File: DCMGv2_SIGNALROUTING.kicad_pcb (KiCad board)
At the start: 2 copper layers, 271.3 x 163.1 mm, 308 parts, among them P1 BRANCH 1 BUS 1 LOAD3 NC, P10 BRANCH 1 BUS 1 LOAD 2 NC, P100 CONNECTOR, P101 CONNECTOR, P102 CONNECTOR, P103 CONNECTOR, P104 CONNECTOR, P105 CONNECTOR, P106 CONNECTOR, P107 CONNECTOR, P108 CONNECTOR, P109 CONNECTOR, P11 BRANCH 1 BUS 1 LOAD 1 NO, P110 CONNECTOR, P111 CONNECTOR, P112 CONNECTOR, P113 CONNECTOR, P114 CONNECTOR, P115 CONNECTOR, P116 CONNECTOR, P117 CONNECTOR, P118 CONNECTOR, P119 CONNECTOR, P12 BRANCH 1 BUS 1 LOAD 1 NC, P120 CONNECTOR, P121 CONNECTOR, P122 CONNECTOR, P123 CONNECTOR, P124 CONNECTOR, P125 CONNECTOR, P126 CONNECTOR, P127 CONNECTOR, P128 CONNECTOR, P129 CONNECTOR, P13 BRANCH 2 BUS 1 LOAD 1 NO, P130 CONNECTOR, P131 CONNECTOR, P132 CONNECTOR, P133 CONNECTOR, P134 CONNECTOR, P135 CONNECTOR, P136 CONNECTOR, P137 CONNECTOR, P138 CONNECTOR, P139 CONNECTOR, P14 BRANCH 2 BUS 1 DISTAL NC, P140 CONNECTOR, P141 CONNECTOR, P142 CONNECTOR, P143 CONNECTOR, P144 CONNECTOR, P145 CONNECTOR, P146 CONNECTOR, P147 CONNECTOR, P148 CONNECTOR, P149 CONNECTOR, P15 BRANCH 2 BUS 1 DISTAL USER, P150 CONNECTOR, P151 CONNECTOR, P152 CONNECTOR, P153 CONNECTOR, P154 CONNECTOR, P155 CONNECTOR, P156 CONNECTOR, P157 CONNECTOR, P158 CONNECTOR, P159 CONNECTOR, P16 BRANCH 2 BUS 1 DISTAL NO, P160 CONNECTOR, P161 CONNECTOR, P162 CONNECTOR, P163 CONNECTOR, P164 CONNECTOR, P165 CONNECTOR, P166 CONNECTOR, P167 CONNECTOR, P168 CONNECTOR, P169 CONNECTOR, P17 BRANCH 2 BUS 1 PROXIMAL NC, P170 CONNECTOR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

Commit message: most traces are triple thickness
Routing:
- net N-0000087: track 55.7 -> 50.0 mm
- net N-0000069: track 50.5 -> 45.2 mm
- net N-0000043: track 139.6 -> 144.6 mm
- net N-0000068: track 67.3 -> 64.8 mm
- net N-0000058: track 92.1 -> 90.0 mm
- net N-0000057: track 91.6 -> 89.9 mm
- net N-0000036: track 89.6 -> 88.3 mm
- net N-0000039: track 90.9 -> 89.7 mm
- net N-0000035: track 89.7 -> 88.5 mm
- net N-0000037: track 89.3 -> 88.3 mm
- net N-0000033: track 91.2 -> 90.1 mm
- net N-0000032: track 91.6 -> 90.6 mm
- net N-0000047: track 91.8 -> 91.0 mm
- net N-0000089: track 34.0 -> 33.4 mm
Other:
- net class thick_signal added: clearance 0.254, trace_width 0.766, via_dia 0.889, via_drill 0.635

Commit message: all traces triple thickness. improved routing
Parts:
- moved P108 7.62 mm to (149.6, 167.4)
- moved P109 7.62 mm to (152.1, 167.4)
- moved P110 7.62 mm to (154.7, 167.4)
- moved P111 7.62 mm to (157.2, 167.4)
- moved P112 7.62 mm to (159.8, 167.4)
- moved P113 7.62 mm to (162.3, 167.4)
- moved P114 7.62 mm to (164.8, 167.4)
- moved P115 7.62 mm to (167.4, 167.4)
- moved P116 7.62 mm to (169.9, 167.4)
- moved P117 7.62 mm to (172.5, 167.4)
- moved P118 7.62 mm to (175.0, 167.4)
- moved P119 7.62 mm to (177.5, 167.4)
- moved P120 7.62 mm to (180.1, 167.4)
- moved P121 7.62 mm to (182.6, 167.4)
- moved P122 7.62 mm to (185.2, 167.4)
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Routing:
- net N-0000059: track 126.2 -> 137.2 mm
- net N-0000042: track 79.3 -> 70.1 mm
- net N-00000131: track 81.1 -> 72.1 mm
- net N-0000044: track 94.5 -> 85.6 mm
- net N-00000122: track 81.4 -> 73.0 mm
- net N-0000040: track 93.3 -> 85.6 mm
- net N-0000045: track 92.8 -> 85.6 mm
- net N-0000047: track 91.0 -> 84.6 mm
- net N-0000032: track 90.6 -> 84.6 mm
- net N-00000145: track 97.4 -> 103.4 mm
- net N-0000033: track 90.1 -> 84.6 mm
- net N-0000058: track 90.0 -> 84.6 mm
- net N-0000057: track 89.9 -> 84.6 mm
- net N-0000039: track 89.7 -> 84.4 mm
- net N-0000086: track 150.7 -> 156.0 mm
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
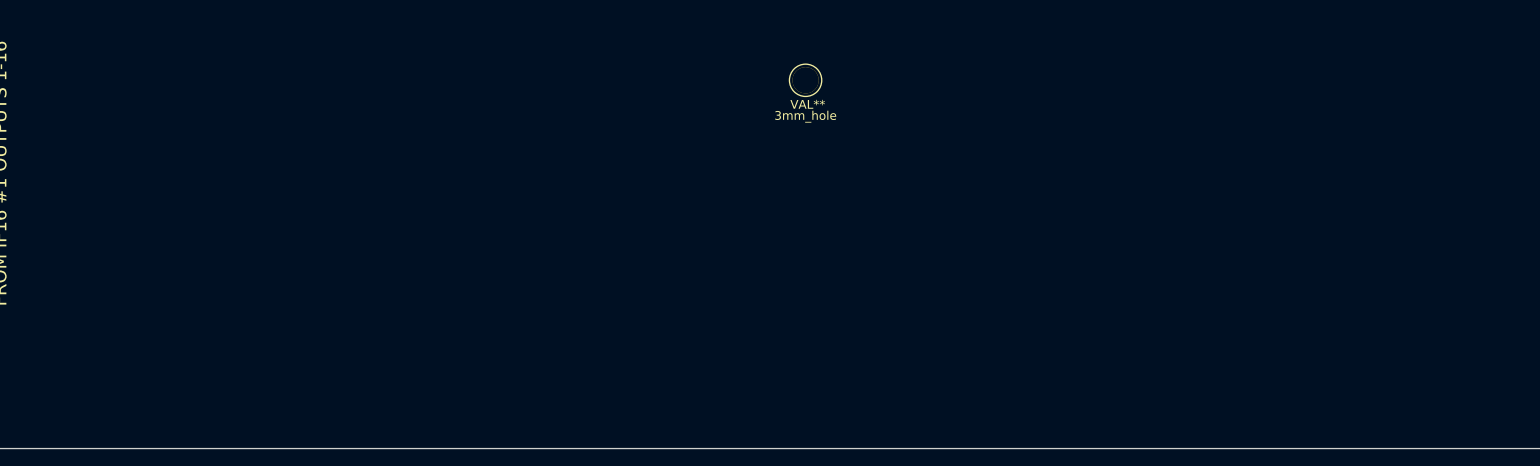
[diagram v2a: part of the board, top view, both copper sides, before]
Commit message: put power circuit on routing board
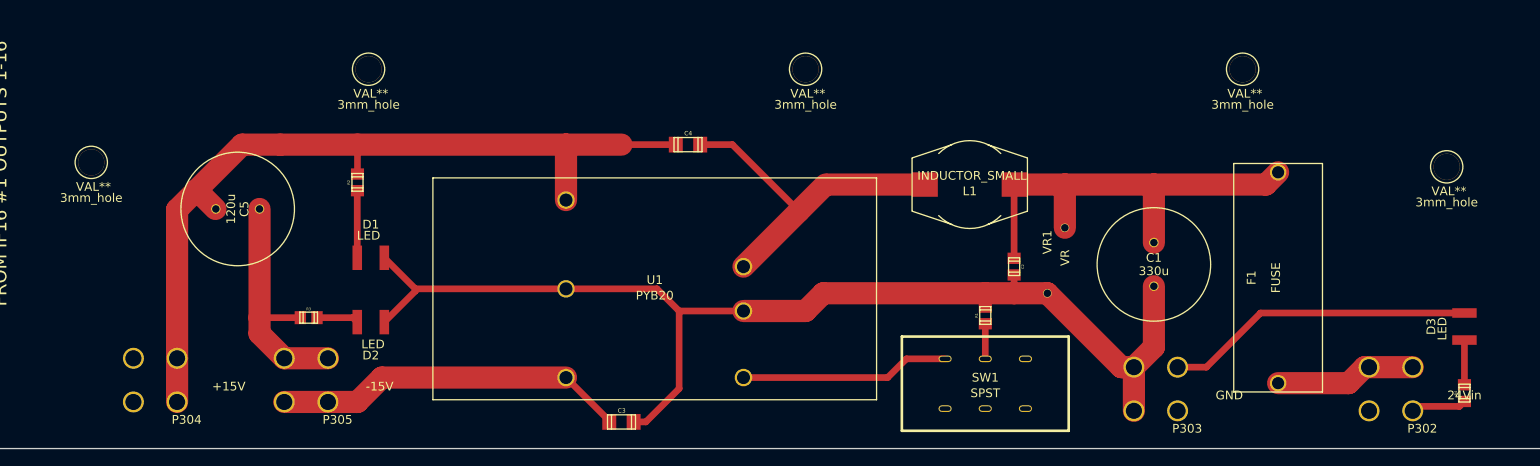
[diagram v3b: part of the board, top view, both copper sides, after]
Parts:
- added 3mm_hole: VAL**, 3mm_hole, F.Cu at (92.2, 192.3)
- added 3mm_hole: VAL**, 3mm_hole, F.Cu at (247.4, 192.8)
- added 3mm_hole: VAL**, 3mm_hole, F.Cu at (224.0, 181.6)
- added 3mm_hole: VAL**, 3mm_hole, F.Cu at (124.0, 181.6)
- added C1: 330u, FR-A_50v, F.Cu at (213.9, 204.0)
- added C2: 1u, c_0805, F.Cu at (197.9, 204.2)
- added C3: C, c_1206, F.Cu at (152.9, 222.0)
- added C4: C, c_1206, F.Cu at (160.5, 190.2)
- added C5: 120u, FR-A_50v, F.Cu at (109.0, 197.6)
- added D1: LED, 1209, F.Cu at (124.2, 203.2)
- added D2: LED, 1209, F.Cu at (124.2, 210.6)
- added D3: LED, 1209, F.Cu at (249.4, 211.1)
- added F1: FUSE, OMNI-BLOCK, F.Cu at (228.1, 205.5)
- added L1: INDUCTOR_SMALL, SDR1005, F.Cu at (192.8, 194.8)
- added P302: 24Vin, Screw Terminal 8191, F.Cu at (238.5, 220.7)
- added P303: GND, Screw Terminal 8191, F.Cu at (211.6, 220.7)
- added P304: +15V, Screw Terminal 8191, F.Cu at (97.0, 219.7)
- added P305: -15V, Screw Terminal 8191, F.Cu at (114.3, 219.7)
- added R1: ctrl pulldown, c_0805, F.Cu at (194.6, 209.8)
- added R2: 2.2k, c_0805, F.Cu at (122.7, 194.6)
- added R3: 2.2k, c_0805, F.Cu at (117.1, 210.1)
- added R4: 2.2k, c_0805, F.Cu at (249.4, 218.7)
- added SW1: SPST, L101011MS02_SPDT, F.Cu at (194.6, 220.5)
- added U1: PYB20, PYB20, F.Cu at (156.7, 206.8)
- added VR1: VR, B722 series, F.Cu at (201.7, 207.3)
- moved 3mm_hole 1.27 mm to (174.0, 181.6)
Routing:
- net N-0000079: track 0.00 -> 168.0 mm
- net N-0000080: track 0.00 -> 95.0 mm
- net N-0000075: track 0.00 -> 68.5 mm
- net N-0000071: track 0.00 -> 50.8 mm
- net N-0000074: track 0.00 -> 39.1 mm
- net N-0000073: track 0.00 -> 24.0 mm
- net N-0000078: track 0.00 -> 22.3 mm
- net N-0000081: track 0.00 -> 7.69 mm
- net N-0000077: track 0.00 -> 5.12 mm
- net N-0000082: track 0.00 -> 4.82 mm
- net N-0000076: track 0.00 -> 4.02 mm
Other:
- net class power added: clearance 0.254, trace_width 2.54, via_dia 0.889, via_drill 0.635

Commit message: improved silk screen labels and reduced board size
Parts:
- moved 3mm_hole 30.7 mm to (82.0, 218.7)
- moved P238 13.4 mm to (55.6, 128.5)
- moved P239 13.4 mm to (55.6, 126.0)
- moved P240 13.4 mm to (55.6, 123.4)
- moved P241 13.4 mm to (55.6, 120.9)
- moved P223 12.7 mm to (55.9, 202.7)
- moved P224 12.7 mm to (55.9, 200.2)
- moved P225 12.7 mm to (55.9, 197.6)
- moved P226 12.7 mm to (55.9, 195.1)
- moved P231 12.7 mm to (55.9, 169.2)
- moved P232 12.7 mm to (55.9, 166.6)
- moved P233 12.7 mm to (55.9, 164.1)
- moved P234 12.7 mm to (55.9, 161.5)
- moved 3mm_hole 11.5 mm to (62.7, 73.4)
- moved P219 4.83 mm to (55.9, 217.4)
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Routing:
- net N-0000023: track 40.0 -> 25.4 mm
- net N-0000022: track 40.0 -> 25.4 mm
- net N-0000020: track 40.0 -> 25.4 mm
- net N-0000021: track 40.0 -> 25.4 mm
- net N-0000030: track 41.7 -> 29.0 mm
- net N-000007: track 33.9 -> 21.2 mm
- net N-000006: track 33.9 -> 21.2 mm
- net N-000005: track 33.9 -> 21.2 mm
- net N-0000032: track 42.3 -> 29.6 mm
- net N-0000029: track 41.7 -> 29.0 mm
- net N-000001: track 33.9 -> 21.2 mm
- net N-0000031: track 42.3 -> 29.6 mm
- net N-000003: track 21.1 -> 23.1 mm
- net N-000002: track 21.1 -> 23.1 mm
- net N-000004: track 21.1 -> 23.1 mm
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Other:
- board size 271.3 x 163.1 mm -> 258.1 x 163.1 mm
- board text added: "+15V OUT"
- board text added: "-15V OUT"
- board text added: "24 V INPUT"
- board text added: "AUX POWER SUPPLY FOR ICS"
- board text added: "GND"
